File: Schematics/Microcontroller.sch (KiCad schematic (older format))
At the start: 25 parts, among them CON1 USB-MICRO-B, IC1 ATXMEGA256A3BU-A, J1 AVR_JTAG_Header, SW1 SW_PUSH, SW2 SW_PUSH, X1 16MHz, X2 32.768KhZ

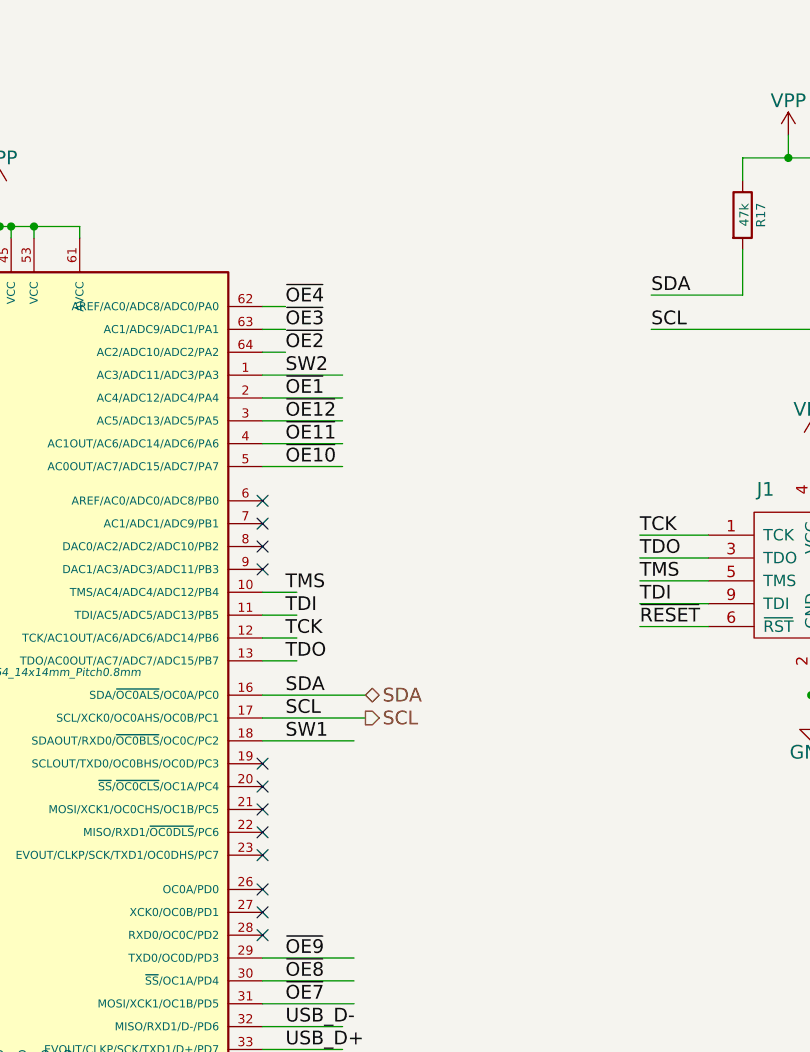
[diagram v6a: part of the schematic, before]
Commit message: Added some debug headers for power and UART
Added silkscreen info also.
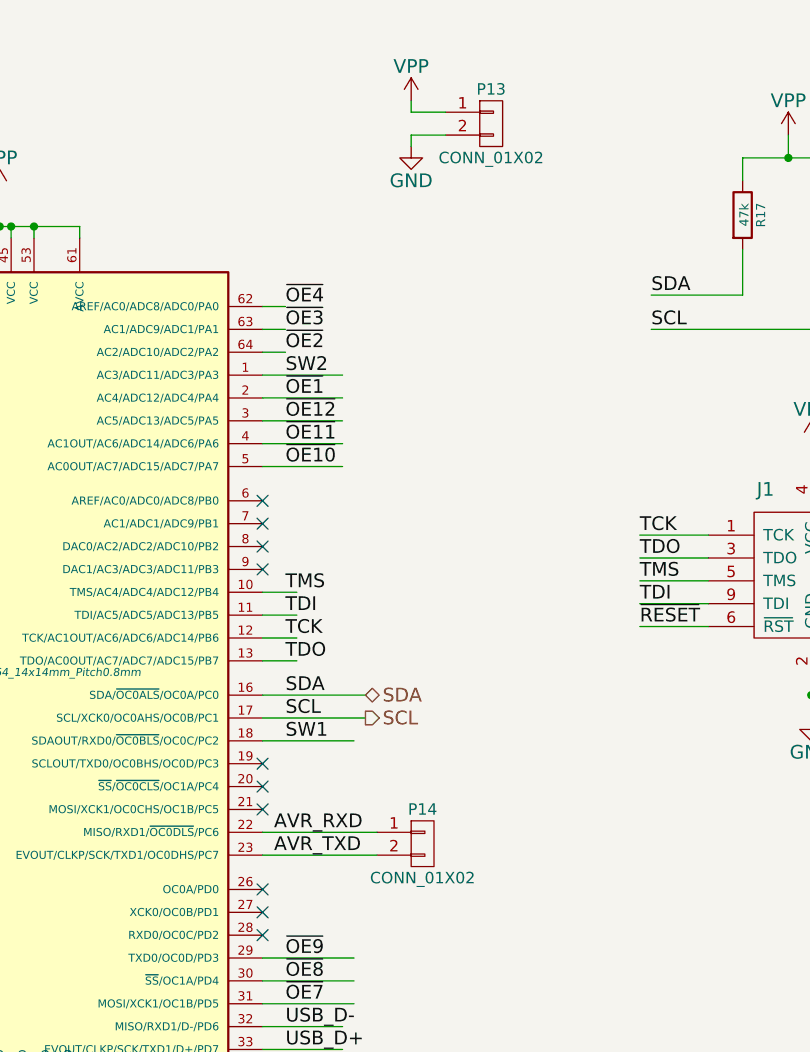
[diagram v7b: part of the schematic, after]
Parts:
- added P13, P14: CONN_01X02, symbol CONN_01X02
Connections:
- net labels added: AVR_RXD, AVR_TXD
- wire segments 133 -> 139
- no-connect marks 24 -> 22
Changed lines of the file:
@@
 SCL
 $Comp
-L VPP #PWR027
+L VPP #PWR29
 U 1 1 54B121F9
 P 9250 1200
-F 0 "#PWR027" H 9250 1050 60  0001 C CNN
+F 0 "#PWR29" H 9250 1050 60  0001 C CNN
 F 1 "VPP" H 9250 1350 60  0000 C CNN
 F 2 "" H 9250 1200 60  0000 C CNN
@@
 $EndComp
 $Comp
-L VPP #PWR028
+L VPP #PWR31
 U 1 1 54B1220F
 P 5800 1450
-F 0 "#PWR028" H 5800 1300 60  0001 C CNN
+F 0 "#PWR31" H 5800 1300 60  0001 C CNN
 F 1 "VPP" H 5800 1600 60  0000 C CNN
 F 2 "" H 5800 1450 60  0000 C CNN
@@
 $EndComp
 $Comp
-L GND #PWR029
+L GND #PWR45
 U 1 1 54B12386
 P 5850 5600
-F 0 "#PWR029" H 5850 5350 60  0001 C CNN
+F 0 "#PWR45" H 5850 5350 60  0001 C CNN
 F 1 "GND" H 5850 5450 60  0000 C CNN
 F 2 "" H 5850 5600 60  0000 C CNN
@@
 TMS
 $Comp
-L VPP #PWR030
+L VPP #PWR35
 U 1 1 54B12F47
 P 9350 2550
-F 0 "#PWR030" H 9350 2400 60  0001 C CNN
+F 0 "#PWR35" H 9350 2400 60  0001 C CNN
 F 1 "VPP" H 9350 2700 60  0000 C CNN
 F 2 "" H 9350 2550 60  0000 C CNN
@@
 $EndComp
 $Comp
-L GND #PWR031
+L GND #PWR42
 U 1 1 54B12FD2
 P 9350 3750
-F 0 "#PWR031" H 9350 3500 60  0001 C CNN
+F 0 "#PWR42" H 9350 3500 60  0001 C CNN
 F 1 "GND" H 9350 3600 60  0000 C CNN
 F 2 "" H 9350 3750 60  0000 C CNN
@@
 TOSC1
 $Comp
-L GND #PWR032
+L GND #PWR39
 U 1 1 54B13B7D
 P 3400 3100
-F 0 "#PWR032" H 3400 2850 60  0001 C CNN
+F 0 "#PWR39" H 3400 2850 60  0001 C CNN
 F 1 "GND" H 3400 2950 60  0000 C CNN
 F 2 "" H 3400 3100 60  0000 C CNN
@@
 $EndComp
 $Comp
-L GND #PWR033
+L GND #PWR40
 U 1 1 54B13BA4
 P 4200 3100
-F 0 "#PWR033" H 4200 2850 60  0001 C CNN
+F 0 "#PWR40" H 4200 2850 60  0001 C CNN
 F 1 "GND" H 4200 2950 60  0000 C CNN
 F 2 "" H 4200 3100 60  0000 C CNN
@@
 $EndComp
 $Comp
-L GND #PWR034
+L GND #PWR43
 U 1 1 54B13F80
 P 3150 3900
-F 0 "#PWR034" H 3150 3650 60  0001 C CNN
+F 0 "#PWR43" H 3150 3650 60  0001 C CNN
 F 1 "GND" H 3150 3750 60  0000 C CNN
 F 2 "" H 3150 3900 60  0000 C CNN
@@
 $EndComp
 $Comp
-L GND #PWR035
+L GND #PWR44
 U 1 1 54B13F86
 P 3950 3900
-F 0 "#PWR035" H 3950 3650 60  0001 C CNN
+F 0 "#PWR44" H 3950 3650 60  0001 C CNN
 F 1 "GND" H 3950 3750 60  0000 C CNN
 F 2 "" H 3950 3900 60  0000 C CNN
@@
 $EndComp
 $Comp
-L GND #PWR036
+L GND #PWR46
 U 1 1 54B15BE6
 P 9250 5850
-F 0 "#PWR036" H 9250 5600 60  0001 C CNN
+F 0 "#PWR46" H 9250 5600 60  0001 C CNN
 F 1 "GND" H 9250 5700 60  0000 C CNN
 F 2 "" H 9250 5850 60  0000 C CNN
@@
 $EndComp
 $Comp
-L GND #PWR037
+L GND #PWR47
 U 1 1 54B15BFC
 P 10450 5850
-F 0 "#PWR037" H 10450 5600 60  0001 C CNN
+F 0 "#PWR47" H 10450 5600 60  0001 C CNN
 F 1 "GND" H 10450 5700 60  0000 C CNN
 F 2 "" H 10450 5850 60  0000 C CNN
@@
 $EndComp
 $Comp
-L GND #PWR038
+L GND #PWR34
 U 1 1 54B17721
 P 3200 2200
-F 0 "#PWR038" H 3200 1950 60  0001 C CNN
+F 0 "#PWR34" H 3200 1950 60  0001 C CNN
 F 1 "GND" H 3200 2050 60  0000 C CNN
 F 2 "" H 3200 2200 60  0000 C CNN
@@
 $EndComp
 $Comp
-L VPP #PWR039
+L VPP #PWR27
 U 1 1 54B284BD
 P 4900 900
-F 0 "#PWR039" H 4900 750 60  0001 C CNN
+F 0 "#PWR27" H 4900 750 60  0001 C CNN
 F 1 "VPP" H 4900 1050 60  0000 C CNN
 F 2 "" H 4900 900 60  0000 C CNN
@@
 $EndComp
 $Comp
-L GND #PWR040
+L GND #PWR32
 U 1 1 54B28C09
 P 4250 1600
-F 0 "#PWR040" H 4250 1350 60  0001 C CNN
+F 0 "#PWR32" H 4250 1350 60  0001 C CNN
 F 1 "GND" H 4250 1450 60  0000 C CNN
 F 2 "" H 4250 1600 60  0000 C CNN
@@
 $EndComp
 $Comp
-L GND #PWR041
+L GND #PWR37
 U 1 1 54B26812
 P 3800 2700
-F 0 "#PWR041" H 3800 2450 60  0001 C CNN
+F 0 "#PWR37" H 3800 2450 60  0001 C CNN
 F 1 "GND" H 3800 2550 60  0000 C CNN
 F 2 "" H 3800 2700 60  0000 C CNN
@@
 $EndComp
 $Comp
-L GND #PWR042
+L GND #PWR41
 U 1 1 54B26B40
 P 3550 3600
-F 0 "#PWR042" H 3550 3350 60  0001 C CNN
+F 0 "#PWR41" H 3550 3350 60  0001 C CNN
 F 1 "GND" H 3550 3450 60  0000 C CNN
 F 2 "" H 3550 3600 60  0000 C CNN
@@
 $EndComp
 $Comp
-L GND #PWR043
+L GND #PWR36
 U 1 1 54B2A340
 P 10550 2550
-F 0 "#PWR043" H 10550 2300 60  0001 C CNN
+F 0 "#PWR36" H 10550 2300 60  0001 C CNN
 F 1 "GND" H 10550 2400 60  0000 C CNN
 F 2 "" H 10550 2550 60  0000 C CNN
@@
 $EndComp
 $Comp
-L VPP #PWR044
+L VPP #PWR33
 U 1 1 54B2B24F
 P 9850 1850
-F 0 "#PWR044" H 9850 1700 60  0001 C CNN
+F 0 "#PWR33" H 9850 1700 60  0001 C CNN
 F 1 "VPP" H 9850 2000 60  0000 C CNN
 F 2 "" H 9850 1850 60  0000 C CNN
@@
 	9400 1300 9400 1400
 $Comp
-L GND #PWR045
+L GND #PWR38
 U 1 1 54C97F8A
 P 2300 3050
-F 0 "#PWR045" H 2300 2800 60  0001 C CNN
+F 0 "#PWR38" H 2300 2800 60  0001 C CNN
 F 1 "GND" H 2300 2900 60  0000 C CNN
 F 2 "" H 2300 3050 60  0000 C CNN
@@
 NoConn ~ 6950 2800
 NoConn ~ 6950 2900
-NoConn ~ 6950 4350
-NoConn ~ 6950 4250
 NoConn ~ 6950 4150
 NoConn ~ 6950 4050
 NoConn ~ 6950 3950
+$Comp
+L CONN_01X02 P14
+U 1 1 55211B60
+P 7650 4300
+F 0 "P14" H 7650 4450 50  0000 C CNN
+F 1 "CONN_01X02" H 7650 4150 50  0000 C CNN
+F 2 "" H 7650 4300 60  0000 C CNN
+F 3 "" H 7650 4300 60  0000 C CNN
+	1    7650 4300
+	1    0    0    -1
+$EndComp
+Wire Wire Line
+	6950 4250 7450 4250
+Wire Wire Line
+	7450 4350 6950 4350
+Text Label 7000 4250 0    60   ~ 0
+AVR_RXD
+Text Label 7000 4350 0    60   ~ 0
+AVR_TXD
+$Comp
+L CONN_01X02 P13
+U 1 1 55212150
+P 7950 1150
+F 0 "P13" H 7950 1300 50  0000 C CNN
+F 1 "CONN_01X02" H 7950 1000 50  0000 C CNN
+F 2 "" H 7950 1150 60  0000 C CNN
+F 3 "" H 7950 1150 60  0000 C CNN
+	1    7950 1150
+	1    0    0    -1
+$EndComp
+$Comp
+L VPP #PWR28
+U 1 1 5521287E
+P 7600 1050
+F 0 "#PWR28" H 7600 900 60  0001 C CNN
+F 1 "VPP" H 7600 1200 60  0000 C CNN
+F 2 "" H 7600 1050 60  0000 C CNN
+F 3 "" H 7600 1050 60  0000 C CNN
+	1    7600 1050
+	1    0    0    -1
+$EndComp
+$Comp
+L GND #PWR30
+U 1 1 552128BF
+P 7600 1250
+F 0 "#PWR30" H 7600 1000 60  0001 C CNN
+F 1 "GND" H 7600 1100 60  0000 C CNN
+F 2 "" H 7600 1250 60  0000 C CNN
+F 3 "" H 7600 1250 60  0000 C CNN
+	1    7600 1250
+	1    0    0    -1
+$EndComp
+Wire Wire Line
+	7750 1100 7600 1100
+Wire Wire Line
+	7600 1100 7600 1050
+Wire Wire Line
+	7600 1250 7600 1200
+Wire Wire Line
+	7600 1200 7750 1200
 $EndSCHEMATC

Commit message: Sorted silkscreen out and panelized design.
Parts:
- P13, P14: footprint (none) -> Pin_Headers:Pin_Header_Straight_1x02
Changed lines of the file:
@@
 LIBS:contrib
 LIBS:valves
+LIBS:JST-SH
 LIBS:pca9685
-LIBS:avr_jtag_header
-LIBS:Root-cache
 EELAYER 25 0
 EELAYER END
@@
 SCL
 $Comp
-L VPP #PWR29
+L VPP #PWR027
 U 1 1 54B121F9
 P 9250 1200
-F 0 "#PWR29" H 9250 1050 60  0001 C CNN
+F 0 "#PWR027" H 9250 1050 60  0001 C CNN
 F 1 "VPP" H 9250 1350 60  0000 C CNN
 F 2 "" H 9250 1200 60  0000 C CNN
@@
 $EndComp
 $Comp
-L VPP #PWR31
+L VPP #PWR028
 U 1 1 54B1220F
 P 5800 1450
-F 0 "#PWR31" H 5800 1300 60  0001 C CNN
+F 0 "#PWR028" H 5800 1300 60  0001 C CNN
 F 1 "VPP" H 5800 1600 60  0000 C CNN
 F 2 "" H 5800 1450 60  0000 C CNN
@@
 $EndComp
 $Comp
-L GND #PWR45
+L GND #PWR029
 U 1 1 54B12386
 P 5850 5600
-F 0 "#PWR45" H 5850 5350 60  0001 C CNN
+F 0 "#PWR029" H 5850 5350 60  0001 C CNN
 F 1 "GND" H 5850 5450 60  0000 C CNN
 F 2 "" H 5850 5600 60  0000 C CNN
@@
 TMS
 $Comp
-L VPP #PWR35
+L VPP #PWR030
 U 1 1 54B12F47
 P 9350 2550
-F 0 "#PWR35" H 9350 2400 60  0001 C CNN
+F 0 "#PWR030" H 9350 2400 60  0001 C CNN
 F 1 "VPP" H 9350 2700 60  0000 C CNN
 F 2 "" H 9350 2550 60  0000 C CNN
@@
 $EndComp
 $Comp
-L GND #PWR42
+L GND #PWR031
 U 1 1 54B12FD2
 P 9350 3750
-F 0 "#PWR42" H 9350 3500 60  0001 C CNN
+F 0 "#PWR031" H 9350 3500 60  0001 C CNN
 F 1 "GND" H 9350 3600 60  0000 C CNN
 F 2 "" H 9350 3750 60  0000 C CNN
@@
 TOSC1
 $Comp
-L GND #PWR39
+L GND #PWR032
 U 1 1 54B13B7D
 P 3400 3100
-F 0 "#PWR39" H 3400 2850 60  0001 C CNN
+F 0 "#PWR032" H 3400 2850 60  0001 C CNN
 F 1 "GND" H 3400 2950 60  0000 C CNN
 F 2 "" H 3400 3100 60  0000 C CNN
@@
 $EndComp
 $Comp
-L GND #PWR40
+L GND #PWR033
 U 1 1 54B13BA4
 P 4200 3100
-F 0 "#PWR40" H 4200 2850 60  0001 C CNN
+F 0 "#PWR033" H 4200 2850 60  0001 C CNN
 F 1 "GND" H 4200 2950 60  0000 C CNN
 F 2 "" H 4200 3100 60  0000 C CNN
@@
 $EndComp
 $Comp
-L GND #PWR43
+L GND #PWR034
 U 1 1 54B13F80
 P 3150 3900
-F 0 "#PWR43" H 3150 3650 60  0001 C CNN
+F 0 "#PWR034" H 3150 3650 60  0001 C CNN
 F 1 "GND" H 3150 3750 60  0000 C CNN
 F 2 "" H 3150 3900 60  0000 C CNN
@@
 $EndComp
 $Comp
-L GND #PWR44
+L GND #PWR035
 U 1 1 54B13F86
 P 3950 3900
-F 0 "#PWR44" H 3950 3650 60  0001 C CNN
+F 0 "#PWR035" H 3950 3650 60  0001 C CNN
 F 1 "GND" H 3950 3750 60  0000 C CNN
 F 2 "" H 3950 3900 60  0000 C CNN
@@
 $EndComp
 $Comp
-L GND #PWR46
+L GND #PWR036
 U 1 1 54B15BE6
 P 9250 5850
-F 0 "#PWR46" H 9250 5600 60  0001 C CNN
+F 0 "#PWR036" H 9250 5600 60  0001 C CNN
 F 1 "GND" H 9250 5700 60  0000 C CNN
 F 2 "" H 9250 5850 60  0000 C CNN
@@
 $EndComp
 $Comp
-L GND #PWR47
+L GND #PWR037
 U 1 1 54B15BFC
 P 10450 5850
-F 0 "#PWR47" H 10450 5600 60  0001 C CNN
+F 0 "#PWR037" H 10450 5600 60  0001 C CNN
 F 1 "GND" H 10450 5700 60  0000 C CNN
 F 2 "" H 10450 5850 60  0000 C CNN
@@
 $EndComp
 $Comp
-L GND #PWR34
+L GND #PWR038
 U 1 1 54B17721
 P 3200 2200
-F 0 "#PWR34" H 3200 1950 60  0001 C CNN
+F 0 "#PWR038" H 3200 1950 60  0001 C CNN
 F 1 "GND" H 3200 2050 60  0000 C CNN
 F 2 "" H 3200 2200 60  0000 C CNN
@@
 $EndComp
 $Comp
-L VPP #PWR27
+L VPP #PWR039
 U 1 1 54B284BD
 P 4900 900
-F 0 "#PWR27" H 4900 750 60  0001 C CNN
+F 0 "#PWR039" H 4900 750 60  0001 C CNN
 F 1 "VPP" H 4900 1050 60  0000 C CNN
 F 2 "" H 4900 900 60  0000 C CNN
@@
 $EndComp
 $Comp
-L GND #PWR32
+L GND #PWR040
 U 1 1 54B28C09
 P 4250 1600
-F 0 "#PWR32" H 4250 1350 60  0001 C CNN
+F 0 "#PWR040" H 4250 1350 60  0001 C CNN
 F 1 "GND" H 4250 1450 60  0000 C CNN
 F 2 "" H 4250 1600 60  0000 C CNN
@@
 $EndComp
 $Comp
-L GND #PWR37
+L GND #PWR041
 U 1 1 54B26812
 P 3800 2700
-F 0 "#PWR37" H 3800 2450 60  0001 C CNN
+F 0 "#PWR041" H 3800 2450 60  0001 C CNN
 F 1 "GND" H 3800 2550 60  0000 C CNN
 F 2 "" H 3800 2700 60  0000 C CNN
@@
 $EndComp
 $Comp
-L GND #PWR41
+L GND #PWR042
 U 1 1 54B26B40
 P 3550 3600
-F 0 "#PWR41" H 3550 3350 60  0001 C CNN
+F 0 "#PWR042" H 3550 3350 60  0001 C CNN
 F 1 "GND" H 3550 3450 60  0000 C CNN
 F 2 "" H 3550 3600 60  0000 C CNN
@@
 $EndComp
 $Comp
-L GND #PWR36
+L GND #PWR043
 U 1 1 54B2A340
 P 10550 2550
-F 0 "#PWR36" H 10550 2300 60  0001 C CNN
+F 0 "#PWR043" H 10550 2300 60  0001 C CNN
 F 1 "GND" H 10550 2400 60  0000 C CNN
 F 2 "" H 10550 2550 60  0000 C CNN
@@
 $EndComp
 $Comp
-L VPP #PWR33
+L VPP #PWR044
 U 1 1 54B2B24F
 P 9850 1850
-F 0 "#PWR33" H 9850 1700 60  0001 C CNN
+F 0 "#PWR044" H 9850 1700 60  0001 C CNN
 F 1 "VPP" H 9850 2000 60  0000 C CNN
 F 2 "" H 9850 1850 60  0000 C CNN
@@
 	9400 1300 9400 1400
 $Comp
-L GND #PWR38
+L GND #PWR045
 U 1 1 54C97F8A
 P 2300 3050
-F 0 "#PWR38" H 2300 2800 60  0001 C CNN
+F 0 "#PWR045" H 2300 2800 60  0001 C CNN
 F 1 "GND" H 2300 2900 60  0000 C CNN
 F 2 "" H 2300 3050 60  0000 C CNN
@@
 F 0 "P14" H 7650 4450 50  0000 C CNN
 F 1 "CONN_01X02" H 7650 4150 50  0000 C CNN
-F 2 "" H 7650 4300 60  0000 C CNN
+F 2 "Pin_Headers:Pin_Header_Straight_1x02" H 7650 4300 60  0001 C CNN
 F 3 "" H 7650 4300 60  0000 C CNN
 	1    7650 4300
@@
 F 0 "P13" H 7950 1300 50  0000 C CNN
 F 1 "CONN_01X02" H 7950 1000 50  0000 C CNN
-F 2 "" H 7950 1150 60  0000 C CNN
+F 2 "Pin_Headers:Pin_Header_Straight_1x02" H 7950 1150 60  0001 C CNN
 F 3 "" H 7950 1150 60  0000 C CNN
 	1    7950 1150
@@
 $EndComp
 $Comp
-L VPP #PWR28
+L VPP #PWR046
 U 1 1 5521287E
 P 7600 1050
-F 0 "#PWR28" H 7600 900 60  0001 C CNN
+F 0 "#PWR046" H 7600 900 60  0001 C CNN
 F 1 "VPP" H 7600 1200 60  0000 C CNN
 F 2 "" H 7600 1050 60  0000 C CNN
@@
 $EndComp
 $Comp
-L GND #PWR30
+L GND #PWR047
 U 1 1 552128BF
 P 7600 1250
-F 0 "#PWR30" H 7600 1000 60  0001 C CNN
+F 0 "#PWR047" H 7600 1000 60  0001 C CNN
 F 1 "GND" H 7600 1100 60  0000 C CNN
 F 2 "" H 7600 1250 60  0000 C CNN
